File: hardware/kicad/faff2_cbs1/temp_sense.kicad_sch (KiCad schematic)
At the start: 0 parts

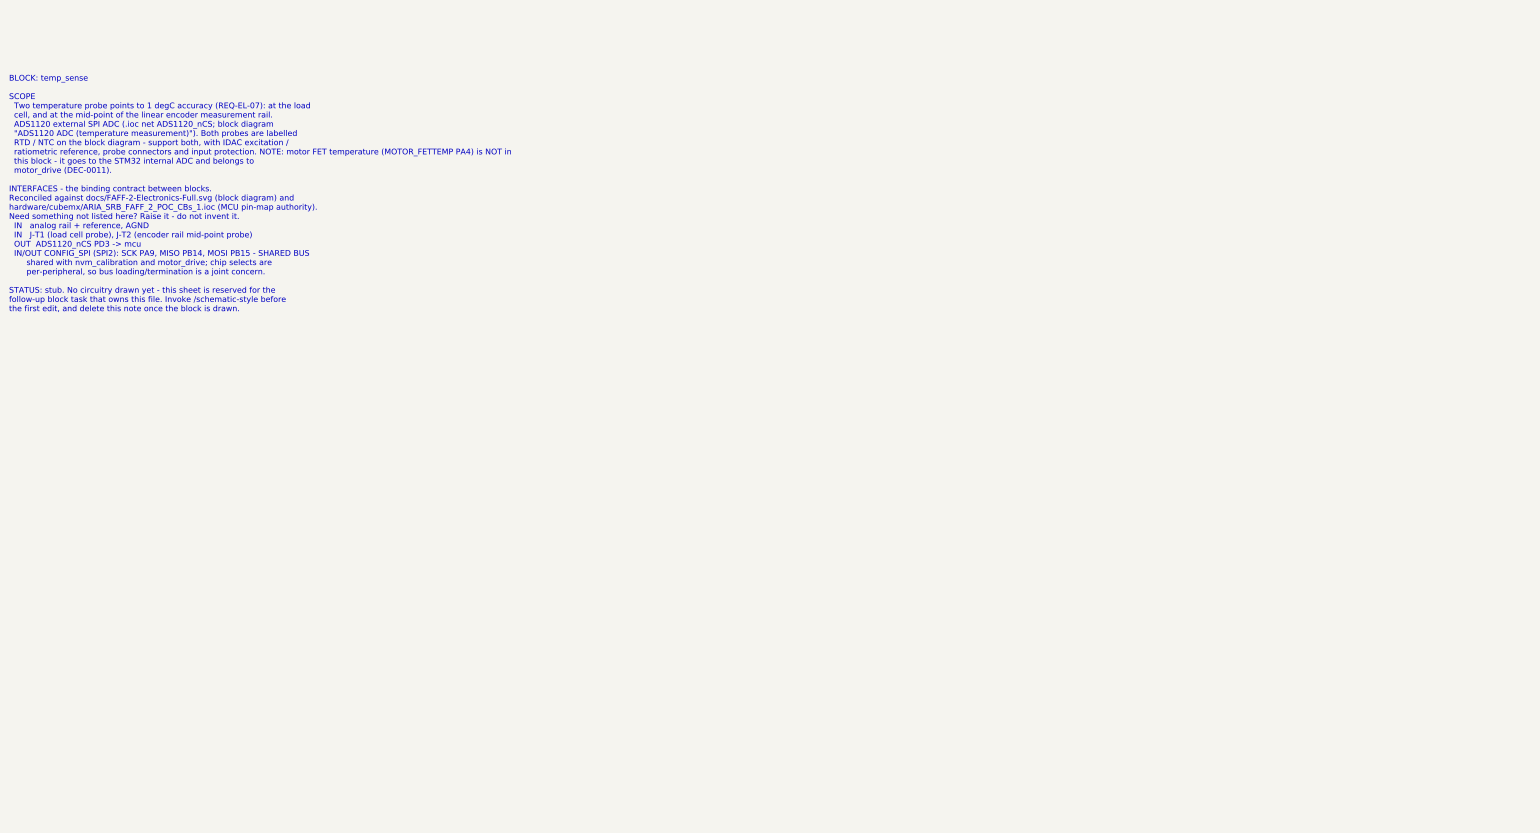
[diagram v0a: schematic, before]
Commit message: temp_sense: two 3-wire Pt1000 channels on one ADS1120; AFE symbol goes local
Draws temp_sense and completes the analog front end. Reasoning, the answer to
OQ-04 and the root-sheet interface list are in docs/decisions/actuator-sch-afe.md.

temp_sense (REQ-EL-07, REQ-AR-10):
  - OQ-04 answered: RTD, not NTC. Pt1000, 3-wire, class A. The ADS1120's two
    matched IDACs exist to excite an RTD ratiometrically and cancel lead
    resistance; a class-A RTD is interchangeable to +/-(0.15 + 0.002|t|) degC
    with no per-part calibration, which an NTC would need to reach 1 degC.
    Pt1000 over Pt100 because every error term here is an error in ohms, and at
    3.85 ohm/degC each costs ten times less in degrees.
  - Both channels share one ADS1120 AND one reference resistor, using the
    datasheet variant (SBAS535D 9.2.2) that routes each IDAC to the pin it
    measures. Its condition - small, well-matched filter resistors - is met with
    100R 0.1%, worth 0.05 degC on a Pt1000.
  - 250 uA IDACs, R707 = 5k 0.05% / 5 ppm, VREF 2.5 V, gain 4. Gain 4 rather
    than 8 keeps the input inside FSR to +200 degC so a probe on warm structure
    cannot silently over-range; resolution is still 0.02 degC. The same board
    takes a Pt100 (the house-stocked probe) with only register changes.
  - Error budget RSS +/-0.28 degC against the 1 degC requirement; the two gain
    terms left out are removed by one-point calibration or IDAC rotation.
  - R708/R709 (DNP) tie the sense lead to the return for a 2-wire probe, which
    keeps the block diagram's "RTD / NTC" option open at lower accuracy.
  - Push-in terminals so a substitute resistor needs no soldering (TEST_PLAN 4).

loadcell_afe: no design change. PWR_FLAGs removed - the power sheets own every
one, and a second flag on a shared rail is a power-output conflict at merge.

Library: AmodoKiCadLib is read-only, so the corrected ADS1235 now lives in
hardware/kicad/faff2_cbs1/faff2_afe.kicad_sym with a sym-lib-table entry, and
the share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
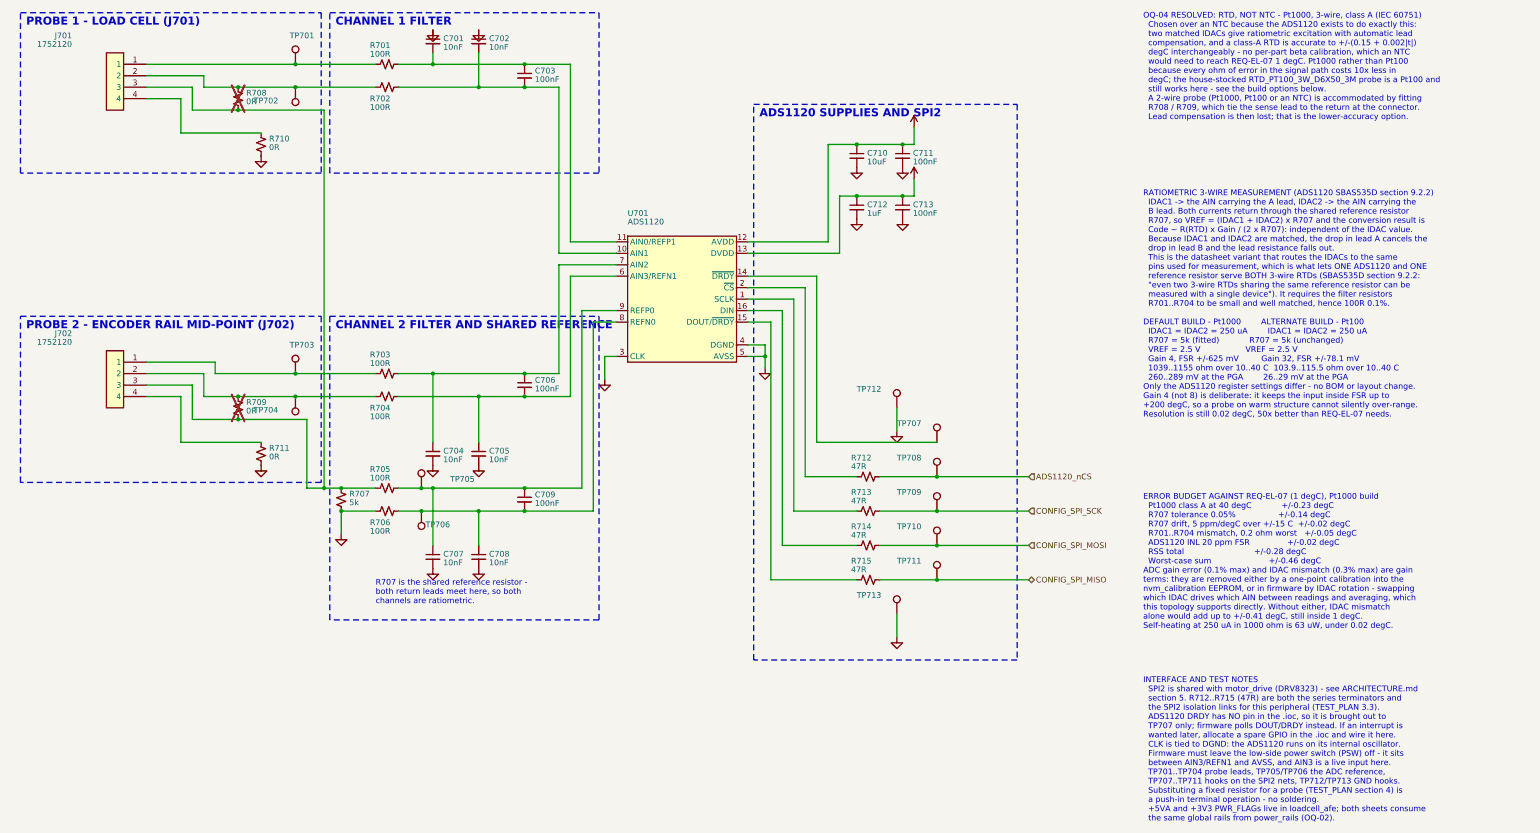
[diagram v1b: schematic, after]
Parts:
- added C701, C702, C704, C705, C707, C708: 10nF, Amodo:C_0603_1608Metric, symbol Amodo_Capacitors:CAP_MLCC_10nF_0603_5%_100V
- added C703, C706, C709, C711, C713: 100nF, Amodo:C_0402_1005Metric, symbol Amodo_Capacitors:CAP_MLCC_100nF_0402_10%_50V
- added C710: 10uF, Amodo:C_0805_2012Metric, symbol Amodo_Capacitors:CAP_MLCC_10uF_0805_20%_25V
- added C712: 1uF, Amodo:C_0603_1608Metric, symbol Amodo_Capacitors:CAP_MLCC_1uF_0603_10%_16V
- added J701, J702: 1752120, Amodo:SHDR4W100P0X350_1X4_1460X1000X1240P, symbol Amodo_Connectors:1752120
- added R701, R702, R703, R704, R705, R706: 100R, Amodo:R_0603_1608Metric, symbol Amodo_Resistors:RES_TNF_100R_0603_0.1%
- added R707: 5k, Amodo:R_0805_2012Metric, symbol Amodo_Resistors:RES_TNF_5k_0805_0.05%
- added R708, R709, R710, R711: 0R, Amodo:R_0603_1608Metric, symbol Amodo_Resistors:RES_TF_0R_0603
- added R712, R713, R714, R715: 47R, Amodo:R_0603_1608Metric, symbol Amodo_Resistors:RES_TF_47R_0603
- added TP701, TP702, TP703, TP704, TP705, TP706: TestPoint, Amodo:TestPoint_Pad_D1.0mm, symbol Amodo_Connectors:TestPoint
- added TP707, TP708, TP709, TP710, TP711, TP712, TP713: TestPoint, Amodo:KeystoneMiniatureTestLoop, symbol Amodo_Connectors:TestPointHook
- added U701: ADS1120, Amodo:TSSOP-16, symbol Amodo_ADCs:ADS1120
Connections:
- new net: J701.2, R702.1, R708.1, TP702.1
- new net: J701.3, J702.3, R705.1, R707.1, R708.2, R709.2
- new net: J702.2, R704.1, R709.1, TP704.1
- new net: C707.1, C709.1, R705.2, TP705.1, U701.9 (REFP0)
- new net: J702.4, R711.1
- new net: J702.1, R703.1, TP703.1
- new net: C702.2, C703.2, R702.2, U701.10 (AIN1)
- new net: J701.1, R701.1, TP701.1
- new net: C701.2, C703.1, R701.2, U701.11 (AIN0/REFP1)
- new net: C705.1, C706.2, R704.2, U701.6 (AIN3/REFN1)
- new net: R713.1, U701.1 (SCLK)
- new net: C704.1, C706.1, R703.2, U701.7 (AIN2)
- new net: J701.4, R710.1
- new net: C708.1, C709.2, R706.2, TP706.1, U701.8 (REFN0)
- new net: R715.1, U701.15 (DOUT/~{DRDY})
- new net: TP707.1, U701.14 (~{DRDY})
- new net: R714.1, U701.16 (DIN)
- new net: R712.1, U701.2 (~{CS})
- new net +3V3: C712.1, C713.1, U701.13 (DVDD)
- new net +5VA: C710.1, C711.1, U701.12 (AVDD)
- new net ADS1120_nCS: R712.2, TP708.1
- new net CONFIG_SPI_MISO: R715.2, TP711.1
- new net CONFIG_SPI_MOSI: R714.2, TP710.1
- new net CONFIG_SPI_SCK: R713.2, TP709.1
- new net GND: C701.1, C702.1, C704.2, C705.2, C707.2, C708.2, C710.2, C711.2, C712.2, C713.2, R706.1, R707.2, R710.2, R711.2, TP712.1, TP713.1, U701.3 (CLK), U701.4 (DGND), U701.5 (AVSS)
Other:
- note added: "ADS1120 SUPPLIES AND SPI2"
- note added: "CHANNEL 1 FILTER"
- note added: "CHANNEL 2 FILTER AND SHARED REFERENCE"
- note added: "ERROR BUDGET AGAINST REQ-EL-07 (1 degC), Pt1000 build Pt1000 class A at 40 degC +/-0.23 degC R707 tolerance 0.05% +/-0.14 degC R707 drift, 5 ppm/degC over +/-15 C +/-0.02 degC R701..R704 mismatch, 0.2 ohm worst +/-0.05 degC ADS1120 INL 20 ppm FSR +/-0.02 degC RSS total +/-0.28 degC Worst-case sum +/-0.46 degC ADC gain error (0.1% max) and IDAC mismatch (0.3% max) are gain terms: they are removed 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"
- note added: "INTERFACE AND TEST NOTES SPI2 is shared with motor_drive (DRV8323) - see ARCHITECTURE.md section 5. R712..R715 (47R) are both the series terminators and the SPI2 isolation links for this peripheral (TEST_PLAN 3.3). ADS1120 DRDY has NO pin in the .ioc, so it is brought out to TP707 only; firmware polls DOUT/DRDY instead. If an interrupt is wanted later, allocate a spare GPIO in the .ioc and wire i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"
- note added: "OQ-04 RESOLVED: RTD, NOT NTC - Pt1000, 3-wire, class A (IEC 60751) Chosen over an NTC because the ADS1120 exists to do exactly this: two matched IDACs give ratiometric excitation with automatic lead compensation, and a class-A RTD is accurate to +/-(0.15 + 0.002|t|) degC interchangeably - no per-part beta calibration, which an NTC would need to reach REQ-EL-07 1 degC. Pt1000 rather than Pt100 bec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"
- note added: "PROBE 1 - LOAD CELL (J701)"
- note added: "PROBE 2 - ENCODER RAIL MID-POINT (J702)"
- note added: "R707 is the shared reference resistor - both return leads meet here, so both channels are ratiometric."
- note added: "RATIOMETRIC 3-WIRE MEASUREMENT (ADS1120 SBAS535D section 9.2.2) IDAC1 -> the AIN carrying the A lead, IDAC2 -> the AIN carrying the B lead. Both currents return through the shared reference resistor R707, so VREF = (IDAC1 + IDAC2) x R707 and the conversion result is Code ~ R(RTD) x Gain / (2 x R707): independent of the IDAC value. Because IDAC1 and IDAC2 are matched, the drop in lead A cancels th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"
- note removed: "BLOCK: temp_sense SCOPE Two temperature probe points to 1 degC accuracy (REQ-EL-07): at the load cell, and at the mid-point of the linear encoder measurement rail. ADS1120 external SPI ADC (.ioc net ADS1120_nCS; block diagram "ADS1120 ADC (temperature measurement)"). Both probes are labelled RTD / NTC on the block diagram - support both, with IDAC excitation / ratiometric reference, probe connect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"
